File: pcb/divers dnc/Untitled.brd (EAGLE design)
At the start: 97.2 x 88 mm, 143 parts, among them IC1 LM2596S, IC2 74ACT244SC, Q1 IRF9321PBF, Q10 FDN337N, Q11 FDN337N, Q12 BSS138, Q13 BSS138, Q14 FDN337N, Q2 BSS670, Q3 BSS138, Q4 BSS670, Q5 BSS138, Q6 BSS316, Q7 BSS138, Q8 BSS138, Q9 BSS670, U1 MAX202CDWR, U2 74HCT595D, U3 TC7SU04F, U4 AL8805WS, U5 AL8805WS, U6 TC7SU04F, X1 USB

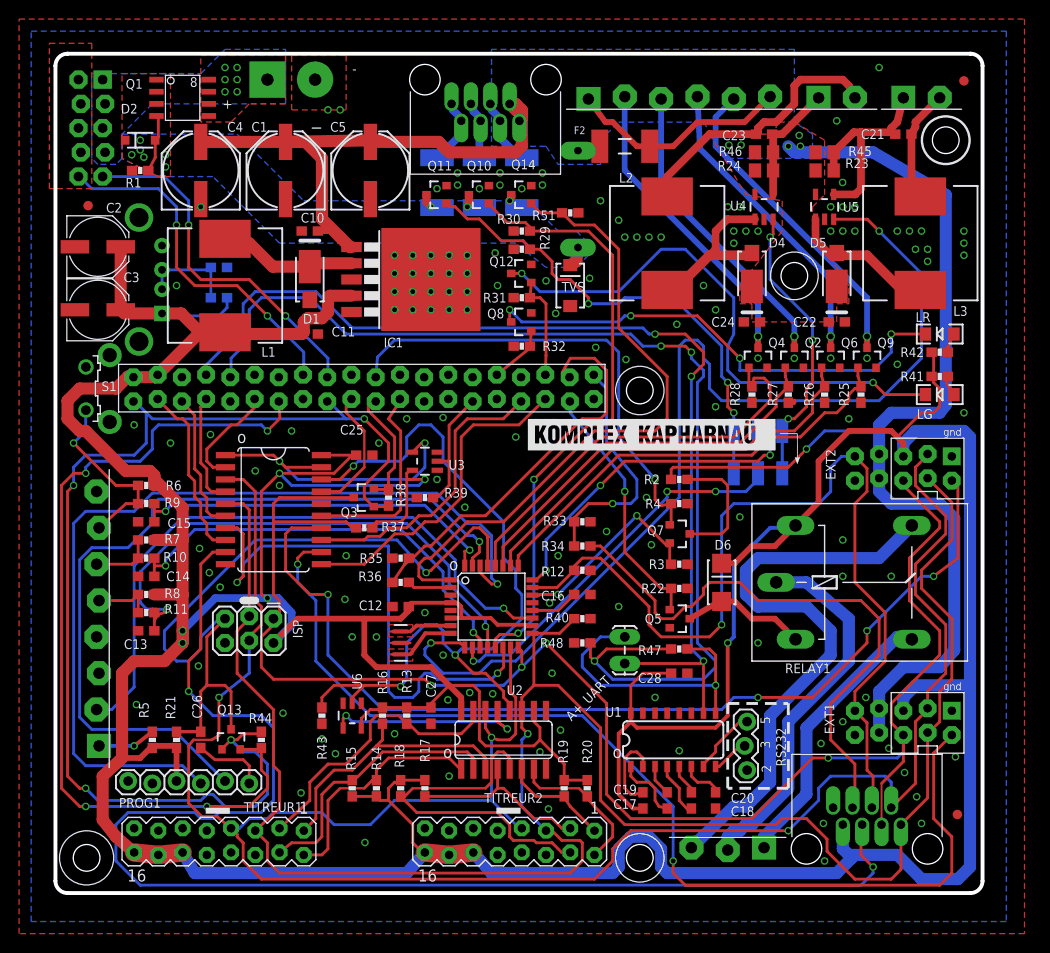
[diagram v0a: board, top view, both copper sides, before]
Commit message: major changes : - carte pieuvre - carte relais - correctif v1 : usb + pin A7 ! - enclosure
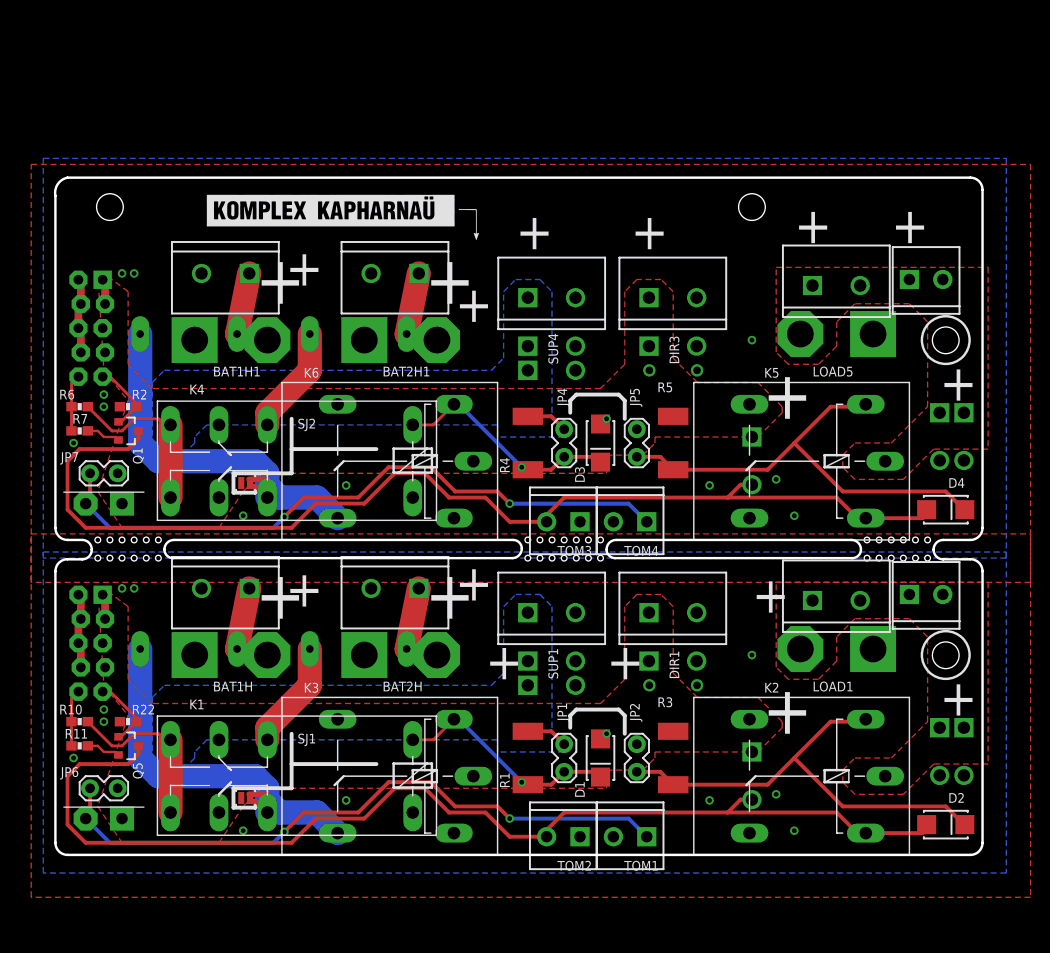
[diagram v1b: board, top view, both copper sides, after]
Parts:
- removed 16MHZ: 16MHZ, SparkFun-FreqCtrl:RESONATOR-SMD
- removed A+_UART: (no value), SparkFun:1X02_LOCK_LONGPADS
- removed AT328: ATMEGA328, SparkFun:TQFP32-08
- removed C10, C11, C12, C16, C17, C18, C19, C20, C22, C24, C25, C26, C27, C28: 0.1uF, rcl:C0603
- removed C13, C14, C15, C21, C23: 1uF, rcl:C0603
- removed C3: 100u, rcl:PANASONIC_D
- removed C4, C5: 220uF, SparkFun:PANASONIC_E
- removed D5: 40v5A, pierre_vv:DO-221
- removed D6: (no value), SparkFun-DiscreteSemi:SMA-DIODE_ALT
- removed EXT1, EXT2: EXT, pierre_vv:EXTPINDNC
- removed F5: PTC1812, pierre_vv:PTC_1812
- removed GYRO-LED: PLUG-6, pierre_vv:PLUG_06
- removed IC1: LM2596S, national-semiconductor:TO263-5
- removed IC2: 74ACT244SC, 74xx-us:SO20W
- removed INPUT: PLUG-8, pierre_vv:PLUG_08
- removed ISP: AVR_SPI_PRG_62X3_LOCK, SparkFun:2X3_LOCK
- removed JP13, JP14, JP19: FIDUCIAL1X2.5, SparkFun:FIDUCIAL-1X2.5
- removed L1: 68nH3A, SparkFun:CDRH125
- removed L2, L3: 100nH2.4A, SparkFun:CDRH125
- removed LED10W1, LED10W2: PLUG-2, pierre_vv:PLUG_02
- removed LG, LR: (no value), SparkFun-LED:LED-1206
- removed PROG1: (no value), SparkFun:1X06_LOCK
- removed Q10, Q11, Q14: FDN337N, SparkFun-DiscreteSemi:SOT23-3
- removed Q12, Q13, Q3, Q7, Q8: BSS138, SparkFun-DiscreteSemi:SOT23-3
- removed Q2, Q4, Q9: BSS670, SparkFun-DiscreteSemi:SOT23-3
- removed Q6: BSS316, SparkFun-DiscreteSemi:SOT23-3
- removed R12: 5.1K, SparkFun-Passives:0603-RES
- removed R13, R14, R15, R16, R17, R18, R19, R20, R25, R26, R27, R28, R29, R30, R31, R32, R51: 100K, SparkFun-Passives:0603-RES
- removed R21, R34, R36, R37, R38, R39, R40, R43, R44, R47: 10K, SparkFun-Passives:0603-RES
- removed R23, R24: 0.110, rcl:R0805
- removed R33, R35, R48: 20K, SparkFun-Passives:0603-RES
- removed R41, R42: 1K, SparkFun-Passives:0603-RES
- removed R45, R46: OPT, rcl:R0805
- removed R49: 22K, SparkFun-Passives:0603-RES
- removed R50, R9: 33K, SparkFun-Passives:0603-RES
- removed R8: 56K, SparkFun-Passives:0603-RES
- removed RAW_IN: DNC_IN2PWR, pierre_vv:DNC_IN2_PWR
- removed RELAY: PLUG-3, pierre_vv:PLUG_03
- removed RELAY1: G5L, relay:G5LE
- removed RGB-LED: RJ45-RGBLED, con-amphenol-rj45-ld:RJ45-TRAFO
- removed RS232: (no value), SparkFun-Connectors:1X03_LOCK
- removed S1: (no value), switch-omron:B3F-31XX
- removed TITREUR1, TITREUR2: DNC_TITREUR, pierre_vv:DNC_TITREUR
- removed TVS: TVS-30V, SparkFun:SMA-DIODE
- removed U$1: RADIATEUR, pierre_vv:RADIATEUR_577102B00000G
- removed U$2: LOGOSIZE2, pierre_vv:KXKMLOGO2
- removed U$4: RASPIA+, pierre_vv:RASPIA+
- removed U$8: RJ45-EXTDNC, con-amphenol-rj45-ld:RJ45-TRAFO
- removed U1: MAX202CDWR, SparkFun-DigitalIC:SO016
- removed U2: 74HCT595D, IC:SO16
- removed U3, U6: TC7SU04F, SparkFun-DigitalIC:SOT23-5
- removed U4, U5: AL8805WS, SparkFun-PowerIC:SOT23-5
- removed X1: USB, pierre_vv:USB_F_SATISTRONIC
- added BAT1, BAT2, BAT3, BAT4, DIR1, DIR2, DIR3, DIR4, EXT-RELAY, EXT-RELAY1, LOAD1, LOAD2, LOAD3, LOAD5, LOAD7, LOAD8, SUP1, SUP2, SUP3, SUP4, SUP5, SUP6: M025MM, SparkFun-Connectors:SCREWTERMINAL-5MM-2
- added BAT1H, BAT1H1, BAT2H, BAT2H1, PLUG_3.81_2_1, PLUG_3.81_2_3: M02HOLE, pierre_vv:2X1_HOLE_BIG
- added D3: (no value), SparkFun-DiscreteSemi:SMA-DIODE_ALT
- added E$1: (no value), pierre_vv:KXKMLOGO2
- added INTER, INTER1: M02PLUG, pierre_vv:PLUG_02
- added JP2, JP4, JP5: 24/12, SparkFun:1X02_LOCK
- added JP3, JP8: CHARGEUR, pierre_vv:2X5_LOCK
- added JP6, JP7: ON, SparkFun:1X02_LOCK
- added K1, K4: 4052, relay:F4052
- added K2, K3, K5, K6: G5L, relay:G5LE
- added LOAD4, LOAD6, TOM1, TOM2, TOM3, TOM4: M023.5MM, SparkFun-Connectors:SCREWTERMINAL-3.5MM-2
- C1: value 220uF -> (none); device SparkFun:PANASONIC_E -> rcl:SANYO-OSCON_9F
- C2: value 100u -> (none); device rcl:PANASONIC_D -> rcl:SANYO-OSCON_9F
- D1, D4: value 40v5A -> (none); device pierre_vv:DO-221 -> SparkFun-DiscreteSemi:SMA-DIODE_ALT
- D2: value 10V -> (none); device SparkFun-DiscreteSemi:SOD-123 -> SparkFun-DiscreteSemi:SMA-DIODE_ALT
- F2, F3, F4: value PTC1812 -> 8A; device pierre_vv:PTC_1812 -> SparkFun:PTC
- JP1: value CHARGEUR -> 24/12; device pierre_vv:2X5_LOCK -> SparkFun:1X02_LOCK
- Q1: value IRF9321PBF -> BSS138; device pierre_vv:SO-8 -> SparkFun-DiscreteSemi:SOT23-3
- R1, R4: value 100K -> 390; device SparkFun-Passives:0603-RES -> rcl:R2512
- R10: value 33K -> 100K
- R11: value 33K -> 10K
- R2: value 100k1% -> 100K
- R3: value 10k1% -> 390; device SparkFun-Passives:0603-RES -> rcl:R2512
- R5: value 1K -> 390; device SparkFun-Passives:0603-RES -> rcl:R2512
- R6: value 56K -> 100K
- R7: value 56K -> 10K
- SJ1, SJ2: value JUMPER-PAD-3-NO -> ONLY BATT; device SparkFun-Passives:PAD-JUMPER-3-NO_YES_SILK_FULL_BOX_WIDE_SPACING -> SparkFun:SJ_2S-NO
- moved D2 110.8 mm to (93.3, 3.17)
- moved JP1 81.5 mm to (53.3, 11.4), turned to 270 degrees
- moved R1 73.8 mm to (49.5, 10.2), turned to 90 degrees
- moved C1 67.6 mm to (64.8, 17.8), flipped to the bottom, turned to 0 degrees
- moved SJ1 66.1 mm to (19.9, 5.97), flipped to the top
- moved R5 62.9 mm to (64.8, 43.2), turned to 90 degrees
- moved F1 62.4 mm to (14.0, 21.6), turned to 180 degrees
- moved C2 61.7 mm to (64.8, 50.8), flipped to the bottom
- moved F2 59.7 mm to (31.8, 21.6), flipped to the bottom, turned to 180 degrees
- moved R22 59.4 mm to (7.62, 14.0), turned to 0 degrees
- moved Q5 59.3 mm to (7.62, 11.4)
- moved D1 58.7 mm to (57.1, 10.2), turned to 270 degrees
- moved R2 58.3 mm to (7.62, 47.0), turned to 0 degrees
- moved SJ2 53.7 mm to (19.9, 39.0), flipped to the top
- moved Q1 35.4 mm to (7.62, 44.5), turned to 270 degrees
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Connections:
- removed net +3V3: Q13.1, Q3.1, R38.2, R44.2, U$4.1, U$4.17
- removed net +5V: AT328.18, AT328.4, AT328.6, C11.1, C12.1, C19.1, C2.+, C25.1, C27.1, C28.1, C3.+, D6.C, EXT1.5V, EXT2.5V, IC1.4, IC2.20, ISP.2, L1.2, PROG1.4, R13.2, R14.2, R15.2, R16.2, R17.2, R18.2, R19.2, R20.2, R21.2, R37.2, R41.2, R42.2, R5.2, R50.1, R6.2, R7.2, R8.2, RELAY1.2, TITREUR1.12, TITREUR1.14, TITREUR1.16, TITREUR2.12, TITREUR2.14, TITREUR2.16, U$4.2, U$4.4, U$8.1, U1.16, U2.10, U2.16, U3.5, U6.5, X1.+
- removed net /REG_RCK_5V=ACTIVE_CS: U2.13, U6.4
- removed net ALL_CS_ENABLE_ACTIVE_LOW_5V: IC2.1, IC2.19, U3.4
- removed net ANALOG_RAW: AT328.22, Q7.2, R3.2
- removed net AREF: AT328.20, C16.1
- removed net ATMEGA_CS: IC2.13, U$4.33
- removed net ATMEGA_CS_5V: AT328.14, IC2.7
- removed net CODE: AT328.23, EXT1.RETOURANALOG, EXT2.RETOURANALOG, R12.1, U$8.6
- removed net CS_TRIGGER_ACTIVE_HIGH: R39.2, U$4.29, U3.2
- removed net DIGITAL_LED2_OR_FLEX3: AT328.24, SJ1.2
- removed net DTR: C26.1, PROG1.1
- removed net EXT1_CS: IC2.8, U$4.3
- removed net EXT1_CS_5V: EXT1./CS, IC2.12
- removed net EXT2_CS: IC2.6, U$4.5
- removed net EXT2_CS_5V: EXT2./CS, IC2.14
- removed net EXT3_CS: IC2.4, U$4.7
- removed net EXT3_CS_5V: IC2.16
- removed net FLOAT1: AT328.19, INPUT.2
- removed net GYRO_1: AT328.28, Q4.1, R28.2
- removed net GYRO_2: AT328.27, Q2.1, R27.2
- removed net GYRO_3: AT328.26, Q6.1, R26.2
- removed net GYRO_4: AT328.25, Q9.1, R25.2
- removed net INT_ATMEGA: R35.2, R36.1, U$4.38
- removed net INT_ATMEGA_5V: AT328.2, R36.2
- removed net INT_TELECO: R33.2, R34.1, U$4.40
- removed net INT_TELECO_5V: R34.2, U$8.4
- removed net LED+1: C23.1, LED10W2.1, R24.1, R46.1, U4.4
- removed net LED+2: C21.1, LED10W1.1, R23.1, R45.1, U5.4
- removed net LED-1: C23.2, L2.2, LED10W2.2
- removed net LED-2: C21.2, L3.2, LED10W1.2
- removed net LEDR: LR.C, Q8.3
- removed net LED_G: Q12.1, R31.2, U$4.36
- removed net LED_R: Q8.1, R32.2, U$4.32
- removed net LG: LG.C, Q12.3
- removed net MISO: Q3.2, R38.1, U$4.21
- removed net MISO_5V: AT328.16, EXT1.MISO, EXT2.MISO, ISP.1, Q3.3, R37.1, U$8.5
- removed net MOSI: IC2.17, U$4.19
- removed net MOSI_5V: AT328.15, EXT1.MOSI, EXT2.MOSI, IC2.3, ISP.4, TITREUR1.7, TITREUR2.7, U$8.8, U2.14
- removed net N$10: GYRO-LED.2, Q4.3
- removed net N$11: GYRO-LED.3, Q2.3
- removed net N$12: GYRO-LED.4, Q6.3
- removed net N$13: GYRO-LED.5, Q9.3
- removed net N$14: F4.2, RGB-LED.7, RGB-LED.8
- removed net N$15: RELAY.3, RELAY1.O
- removed net N$16: D6.A, Q5.3, RELAY1.1
- removed net N$17: F4.1, Q11.3
- removed net N$18: LG.A, R41.1
- removed net N$19: F3.1, Q10.3
- removed net N$20: INPUT.6, R10.1, R7.1
- removed net N$21: LR.A, R42.1
- removed net N$22: INPUT.7, R6.1, R9.1, S1.2
- removed net N$23: INPUT.5, R11.1, R8.1
- removed net N$24: C19.2, U1.2
- removed net N$25: INPUT.1, R5.1
- removed net N$26: R49.2, R50.2, X1.DM, X1.DP
- removed net N$29: F5.2, RGB-LED.3, RGB-LED.4
- removed net N$30: F5.1, Q14.3
- removed net N$35: C20.1, U1.6
- removed net N$43: 16MHZ.1, AT328.7
- removed net N$44: 16MHZ.3, AT328.8
- removed net N$50: C18.2, U1.5
- removed net N$51: C18.1, U1.4
- removed net N$52: C17.2, U1.3
- removed net N$53: C17.1, U1.1
- removed net N$9: F3.2, RGB-LED.5, RGB-LED.6
- removed net PROTECT_GATE: D2.A, Q1.4, R1.1
- removed net PRXD_PIN2_RS232: RS232.1, U1.7
- removed net PTXD_PIN3_RS232: RS232.2, U1.8
- removed net PUSH1: AT328.32, C15.1, R9.2
- removed net PUSH2: AT328.11, C14.1, R10.2
- removed net PUSH3: AT328.12, C13.1, R11.2
- removed net PWM_FLEX_1: AT328.1, Q14.1, R51.2
- removed net PWM_FLEX_2: AT328.13, Q10.1, R30.2
- removed net PWM_FLEX_3: Q11.1, R29.2, SJ1.3, SJ2.3
- removed net PWM_LED2_OR_FLEX3: AT328.10, SJ2.2
- removed net PWM_LED_1: AT328.9, U5.3
- removed net PWM_LED_2: SJ1.1, SJ2.1, U4.3
- removed net RAW_FUSED: C1.+, C10.1, C22.1, C24.1, C4.+, C5.+, D4.C, D5.C, EXT1.RAW, EXT1.RAW2, EXT2.RAW, EXT2.RAW2, F1.P$2, F2.1, IC1.1, R2.2, R23.2, R24.2, R45.2, R46.2, RGB-LED.1, RGB-LED.2, U4.5, U5.5
- removed net RAW_POL_PROTECTED: D2.C, F1.P$1MOV, Q1.1, Q1.2, Q1.3, TVS.C
- removed net RAW_UNPROTECTED: JP1.3, JP1.5, JP1.7, JP1.9, Q1.5, Q1.6, Q1.7, Q1.8, RAW_IN.1
- removed net READ_BATTERY: Q7.1, R4.2, U$4.22
- removed net REG_RCK: IC2.2, U$4.11
- removed net REG_RCK_5V: IC2.18, R43.2, U2.12, U6.2
- removed net RELAY1: Q5.1, R22.2, U$4.37
- removed net RESET: Q13.2, R44.1, U$4.13
- removed net RESET_5V: AT328.29, C26.2, ISP.5, Q13.3, R21.1
- removed net RST1: R16.1, TITREUR1.1, U2.3
- removed net RST2: R14.1, TITREUR1.2, U2.1
- removed net RST3: R13.1, TITREUR1.3, U2.15
- removed net RST4: R15.1, TITREUR1.4, U2.2
- removed net RST5: R19.1, TITREUR2.1, U2.6
- removed net RST6: R20.1, TITREUR2.2, U2.7
- removed net RST7: R17.1, TITREUR2.3, U2.4
- removed net RST8: R18.1, TITREUR2.4, U2.5
- removed net RX-I: AT328.30, PROG1.3
- removed net RXA+: R47.1, R48.2, U$4.10
- removed net RXA+_5V: A+_UART.2, R47.2, U1.9
- removed net SCK: IC2.15, U$4.23
- removed net SCK_5V: AT328.17, EXT1.SCK, EXT2.SCK, IC2.5, ISP.3, R40.2, TITREUR1.5, TITREUR2.5, U$8.7, U2.11
- removed net TELECO_CS: IC2.11, U$4.35
- removed net TELECO_CS_5V: IC2.9, U$8.3
- removed net TX-O: AT328.31, PROG1.2
- removed net TXA+_5V: A+_UART.1, U$4.8, U1.10
- new net +TOM: INTER.2, JP6.1, TOM1.1
- new net +TOM1: INTER1.2, JP7.1, TOM4.1
- new net BATT1: F1.P$1MOV, K1.O2, K3.O, SJ1.2
- new net BATT2: F2.P$1MOV, K1.O1
- new net BATT3: F3.P$1MOV, K4.O2, K6.O, SJ2.2
- new net BATT4: F4.P$1MOV, K4.O1
- new net CHARGING1: JP8.2, R6.1, R7.2
- new net GND1: BAT1H1._, BAT2H1._, BAT3.2, BAT4.2, C2.-, D3.A, DIR3.2, DIR4.2, JP8.10, JP8.4, JP8.6, JP8.8, K4.1, K6.2, LOAD5.2, LOAD6.2, LOAD7.2, LOAD8.2, PLUG_3.81_2_1._, Q1.2, R2.1, R7.1, SUP4.2, SUP5.2, SUP6.2, TOM4.2
- new net LOAD: K2.P, LOAD1.1, LOAD2.1, LOAD3.1, LOAD4.1, PLUG_3.81_2_3.+
- new net LOAD1: K5.P, LOAD5.1, LOAD6.1, LOAD7.1, LOAD8.1, PLUG_3.81_2_1.+
- new net N$2: BAT1.1, BAT1H.+, F1.P$2
- new net RELAY_CHARGE_BOARD1: JP8.1, Q1.1, R2.2
- new net SINK_FROM_TOM: D2.A, EXT-RELAY.2, K2.2, Q5.3, TOM2.2
- new net SINK_FROM_TOM1: D4.A, EXT-RELAY1.2, K5.2, Q1.3, TOM3.2
- new net SUPPLY: JP1.1, K1.S1, K1.S2, K3.S, R1.2, R10.2, SUP1.1, SUP2.1, SUP3.1
- new net SUPPLY/BATT: C1.+, DIR1.1, DIR2.1, EXT-RELAY.1, INTER.1, JP2.1, JP3.3, JP3.5, JP3.7, JP3.9, JP6.2, K1.P1, K1.P2, K2.S, K3.P, R3.2, SJ1.1
- new net SUPPLY/BATT1: C2.+, DIR3.1, DIR4.1, EXT-RELAY1.1, INTER1.1, JP5.1, JP7.2, JP8.3, JP8.5, JP8.7, JP8.9, K4.P1, K4.P2, K5.S, K6.P, R5.2, SJ2.1
- new net SUPPLY1: JP4.1, K4.S1, K4.S2, K6.S, R4.2, R6.2, SUP4.1, SUP5.1, SUP6.1
- net CHARGING: now also JP3.2, R10.1, R11.2; no longer JP1.2, U$4.16
- net GND: now also BAT1.2, BAT1H._, BAT2.2, BAT2H._, DIR1.2, DIR2.2, JP3.10, JP3.4, JP3.6, JP3.8, K1.1, K3.2, LOAD1.2, LOAD2.2, LOAD3.2, LOAD4.2, PLUG_3.81_2_3._, R11.1, SUP1.2, SUP2.2, SUP3.2, TOM1.2; no longer 16MHZ.2, AT328.21, AT328.3, AT328.5, C10.2, C11.2, C12.2, C13.2, C14.2, C15.2, C16.2, C2.-, C20.2, C22.2, C24.2, C25.2, C27.2, C28.2, C3.-, C4.-, C5.-, EXT1.1_GND, EXT1.GND2, EXT2.1_GND, EXT2.GND2, IC1.3, IC1.5, IC1.THERMAL, IC2.10, INPUT.4, INPUT.8, ISP.6, JP1.10, JP1.4, JP1.6, JP1.8, PROG1.5, PROG1.6, Q10.2, Q11.2, Q12.2, Q14.2, Q2.2, Q4.2, Q6.2, Q8.2, Q9.2, R1.2, R12.2, R25.1, R26.1, R27.1, R28.1, R29.1, R3.1, R30.1, R31.1, R32.1, R33.1, R35.1, R39.1, R4.1, R40.1, R43.1, R48.1, R49.1, R51.1, RAW_IN.2, RS232.3, S1.1, TITREUR1.11, TITREUR1.13, TITREUR1.15, TITREUR1.8, TITREUR2.11, TITREUR2.13, TITREUR2.15, TITREUR2.8, TVS.A, U$4.14, U$4.20, U$4.25, U$4.30, U$4.34, U$4.39, U$4.6, U$4.9, U$8.2, U1.15, U2.8, U3.3, U4.2, U5.2, U6.3, X1.-, X1.S1, X1.S2
- net N$1: now also JP1.2, K1.2, K3.1, R1.1; no longer IC1.2, L1.1
- net N$3: now also BAT2.1, BAT2H.+, F2.P$2; no longer Q7.3, R2.1
- net N$4: now also D2.C, JP2.2, K2.1, R3.1; no longer RELAY.1, RELAY1.S
- net N$5: now also D3.C, JP4.2, K4.2, K6.1, R4.1; no longer F2.2, GYRO-LED.1, GYRO-LED.6
- net N$6: now also D4.C, JP5.2, K5.1, R5.1; no longer D4.A, L2.1, U4.1
- net N$7: now also BAT1H1.+, BAT3.1, F3.P$2; no longer D5.A, L3.1, U5.1
- net N$8: now also BAT2H1.+, BAT4.1, F4.P$2; no longer RELAY.2, RELAY1.P
- net RELAY_CHARGE_BOARD: now also JP3.1, Q5.1, R22.2; no longer JP1.1, U$4.18
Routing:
- net +5V: track 579.0 -> 0.00 mm, vias 6 -> 0
- net MOSI_5V: track 227.8 -> 0.00 mm, vias 3 -> 0
- net SCK_5V: track 211.8 -> 0.00 mm, vias 1 -> 0
- net RAW_FUSED: track 180.6 -> 0.00 mm, vias 6 -> 0
- net MISO_5V: track 169.7 -> 0.00 mm, vias 4 -> 0
- net TELECO_CS_5V: track 143.6 -> 0.00 mm, vias 2 -> 0
- net +3V3: track 123.3 -> 0.00 mm, vias 4 -> 0
- net RXA+: track 116.4 -> 0.00 mm, vias 3 -> 0
- net SINK_FROM_TOM1: track 0.00 -> 116.0 mm
- net SINK_FROM_TOM: track 0.00 -> 116.0 mm
- net EXT1_CS_5V: track 111.4 -> 0.00 mm, vias 2 -> 0
- net PWM_LED_1: track 109.1 -> 0.00 mm, vias 2 -> 0
- net TXA+_5V: track 108.2 -> 0.00 mm, vias 3 -> 0
- net EXT2_CS_5V: track 103.6 -> 0.00 mm, vias 4 -> 0
- net CODE: track 97.4 -> 0.00 mm, vias 1 -> 0
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- added copper zone on layer 1, net GND1
- added copper zone on layer 16, net GND1
- added copper zone on layer 1, net LOAD
- added copper zone on layer 1, net LOAD1
- added copper zone on layer 16, net SUPPLY
- added copper zone on layer 1, net SUPPLY/BATT
- added copper zone on layer 1, net SUPPLY/BATT1
- added copper zone on layer 16, net SUPPLY1
- removed copper zone on layer 1, net N$27
- removed copper zone on layer 1, net N$28
- removed copper zone on layer 1, net RAW_FUSED
- removed copper zone on layer 16, net RAW_FUSED
- removed copper zone on layer 1, net RAW_POL_PROTECTED
- removed copper zone on layer 16, net RAW_POL_PROTECTED
- removed copper zone on layer 1, net RAW_UNPROTECTED
- removed copper zone on layer 16, net RAW_UNPROTECTED
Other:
- board size 97.2 x 88 mm -> 97.2 x 71 mm
- board text added: "BAT1"
- board text added: "BAT1H"
- board text added: "BAT2"
- board text added: "BAT2H"
- board text added: "C1"
- board text added: "D1"
- board text added: "D2"
- board text added: "DIR1"
- board text added: "DIR2"
- board text added: "EXT-RELAY"
- board text added: "F1"
- board text added: "F2"
- board text added: "JP1"
- board text added: "JP2"
- board text added: "JP6"
- board text added: "K1"
- board text added: "K2"
- board text added: "K3"
- board text added: "LOAD1"
- board text added: "LOAD2"
- board text added: "LOAD4"
- board text added: "Q5"
- board text added: "R1"
- board text added: "R10"
- board text added: "R11"
- board text added: "R22"
- board text added: "R3"
- board text added: "SJ1"
- board text added: "SUP1"
- board text added: "SUP2"
- board text added: "SUP3"
- board text added: "TOM1"
- board text added: "TOM2"
- board text removed: "-"
- board text removed: "2"
- board text removed: "3"
- board text removed: "5"
- board text removed: "5V IPOD"
- board text removed: "BRD+10mm"
- board text removed: "BRD+13,5mm"
- board text removed: "BRD+4mm diam4mm"
- board text removed: "BRD+8mm"
- board text removed: "CARTE DNC V0.3"
- board text removed: "DIGITAL"
- board text removed: "FLEX B"
- board text removed: "LED 10W 2"
- board text removed: "PWM"
- board text removed: "Pierre H Olivier R"
- board text removed: "RPI+3mm"
- board text removed: "RPI+3mm diam15mm"
- board text removed: "RPI+6mm"
- board text removed: "RPI+7mm"
- board text removed: "RPI-2mm"
- board text removed: "fev 2015"
- board text removed: "o"
- board text removed: "titreur BRD+7mm"
